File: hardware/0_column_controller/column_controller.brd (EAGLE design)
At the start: 35.6 x 54.6 mm, 45 parts, among them J4 JTAG, U1 ESP-WROVER-32ESP-WROVER-32, U2 3.3V, U3 CP2102N

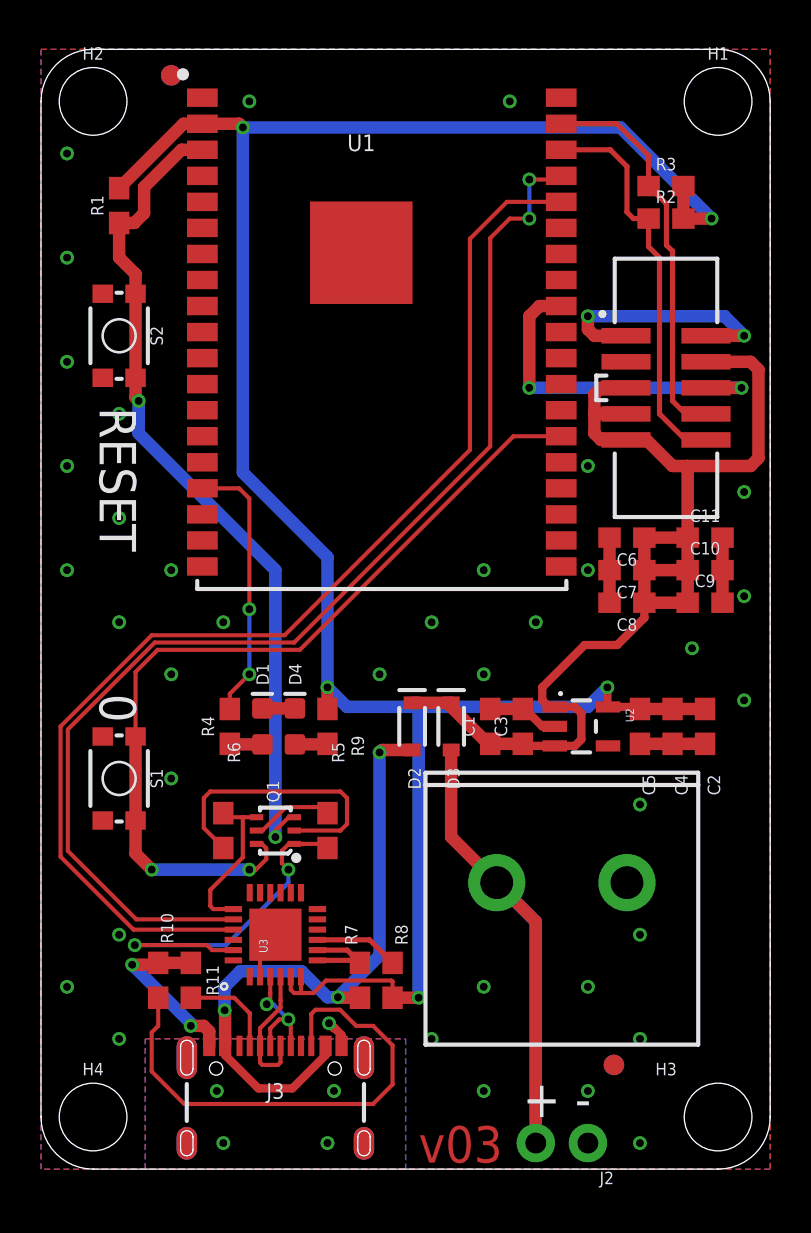
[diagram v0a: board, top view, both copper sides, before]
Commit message: increase standoff size column controller
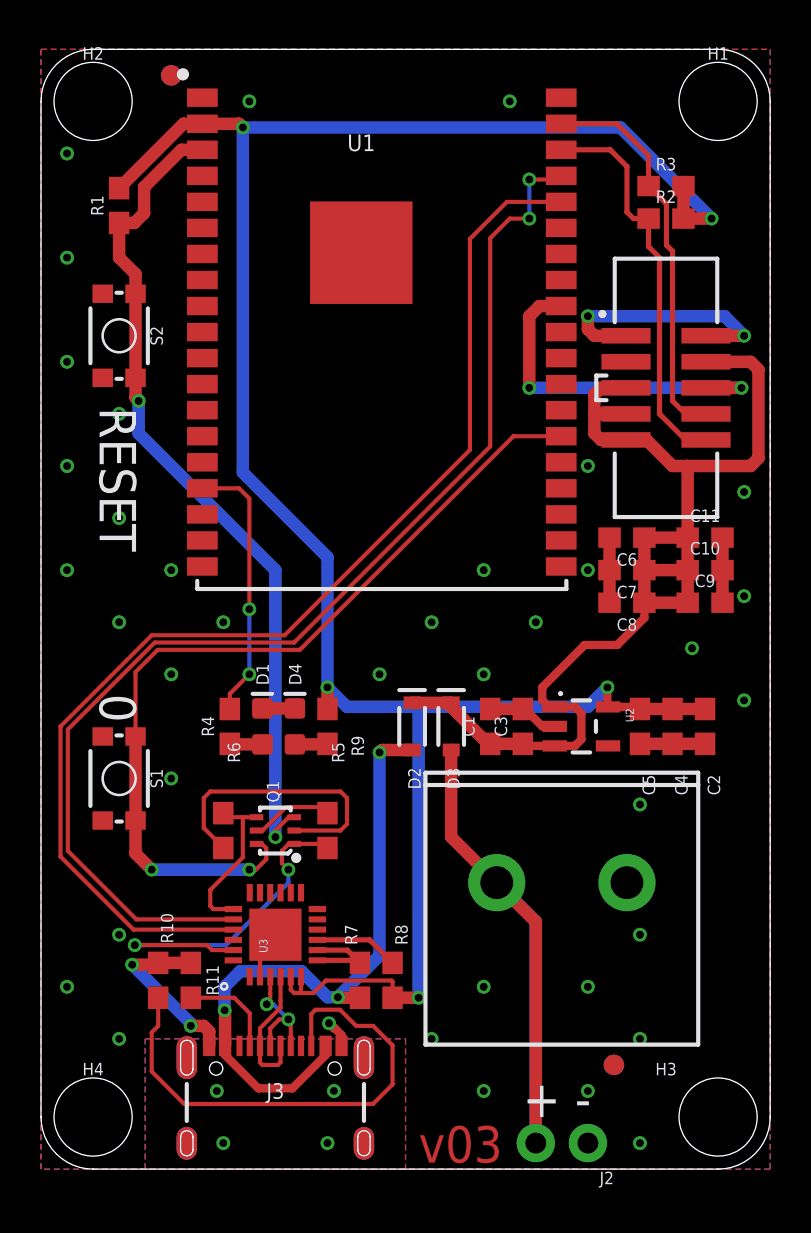
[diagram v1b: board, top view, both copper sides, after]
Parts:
- H1, H2, H3, H4: value STAND-OFF -> STAND-OFF#8; device SparkFun-Hardware:STAND-OFF -> standoff:STAND-OFF-#8
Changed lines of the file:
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@@
 <attribute name="VALUE" x="27.94" y="3.302" size="0.6096" layer="27" font="vector" ratio="20" rot="R180"/>
 </element>
-<element name="H1" library="SparkFun-Hardware" package="STAND-OFF" value="STAND-OFF" x="33.02" y="52.07" smashed="yes">
+<element name="H1" library="standoff" package="STAND-OFF-#8" value="STAND-OFF#8" x="33.02" y="52.07" smashed="yes">
 <attribute name="NAME" x="33.02" y="54.102" size="0.6096" layer="25" font="vector" ratio="20" align="bottom-center"/>
 <attribute name="VALUE" x="29.21" y="46.228" size="0.6096" layer="27" font="vector" ratio="20" align="top-center"/>
 </element>
-<element name="H2" library="SparkFun-Hardware" package="STAND-OFF" value="STAND-OFF" x="2.54" y="52.07" smashed="yes">
+<element name="H2" library="standoff" package="STAND-OFF-#8" value="STAND-OFF#8" x="2.54" y="52.07" smashed="yes">
 <attribute name="NAME" x="2.54" y="54.102" size="0.6096" layer="25" font="vector" ratio="20" align="bottom-center"/>
 <attribute name="VALUE" x="2.54" y="50.038" size="0.6096" layer="27" font="vector" ratio="20" align="top-center"/>
 </element>
-<element name="H3" library="SparkFun-Hardware" package="STAND-OFF" value="STAND-OFF" x="33.02" y="2.54" smashed="yes">
+<element name="H3" library="standoff" package="STAND-OFF-#8" value="STAND-OFF#8" x="33.02" y="2.54" smashed="yes">
 <attribute name="NAME" x="30.48" y="4.572" size="0.6096" layer="25" font="vector" ratio="20" align="bottom-center"/>
 <attribute name="VALUE" x="33.02" y="0.508" size="0.6096" layer="27" font="vector" ratio="20" align="top-center"/>
 </element>
-<element name="H4" library="SparkFun-Hardware" package="STAND-OFF" value="STAND-OFF" x="2.54" y="2.54" smashed="yes">
+<element name="H4" library="standoff" package="STAND-OFF-#8" value="STAND-OFF#8" x="2.54" y="2.54" smashed="yes">
 <attribute name="NAME" x="2.54" y="4.572" size="0.6096" layer="25" font="vector" ratio="20" align="bottom-center"/>
 <attribute name="VALUE" x="2.54" y="0.508" size="0.6096" layer="27" font="vector" ratio="20" align="top-center"/>

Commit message: prepare for v10 generation
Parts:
- J1: device SparkFun-Connectors:1X02_6.35_SCREWTERM -> SparkFun-Connectors:SCREWTERMINAL-3.5MM-4_LOCK
- R2, R3: value 2.2k -> 1k
- R4, R9: value 33 -> 330
- moved J1 4.58 mm to (22.9, 10.2)
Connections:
- net GND: now also J1.3, J1.4; no longer J1.P2
- net VIN: now also J1.1, J1.2; no longer J1.P1
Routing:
- net VIN: track 34.4 -> 38.9 mm
- net GND: vias 42 -> 39
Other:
- board text added: "v10"
- board text removed: "v03"

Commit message: update controller board
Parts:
- removed FRAME1: FRAME-LEDGER, SparkFun-Aesthetics:CREATIVE_COMMONS
- removed J2: (no value), SparkFun-Connectors:1X02_NO_SILK
- added U$1: (no value), buzzard_labels:5V2
- added U$10: (no value), buzzard_labels:SUMMER_202010
- added U$11: (no value), buzzard_labels:#PLAYZEUM#10
- added U$12: (no value), SparkFun-Aesthetics:OSHW-LOGO-M
- added U$2: (no value), buzzard_labels:#GND#6
- added U$3: (no value), buzzard_labels:#13#0
- added U$4: (no value), buzzard_labels:#USER#2
- added U$5: (no value), buzzard_labels:#RESET#3
- added U$6: (no value), ocl_L#PNG:OCL_L#PNG
- added U$7: (no value), buzzard_labels:MUSEUM_OF_BOULDER9
- added U$8: (no value), buzzard_labels:OCLYKE#DEV7
- added U$9: (no value), buzzard_labels:#RAINBOW_FOREST#8
- moved J1 1.80 mm to (21.6, 11.4)
- moved H1 1.27 mm to (33.0, 53.3)
- moved H2 1.27 mm to (2.54, 53.3)
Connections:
- net GND: no longer J2.1
- net VIN: no longer J2.2
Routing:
- net VIN: track 38.9 -> 17.3 mm
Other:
- board size 35.6 x 54.6 mm -> 35.6 x 55.9 mm
- board text removed: "+"
- board text removed: "-"
- board text removed: "0"
- board text removed: "RESET"

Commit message: add frame and organize
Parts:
- added FRAME1: FRAME-LETTER, SparkFun-Aesthetics:CREATIVE_COMMONS

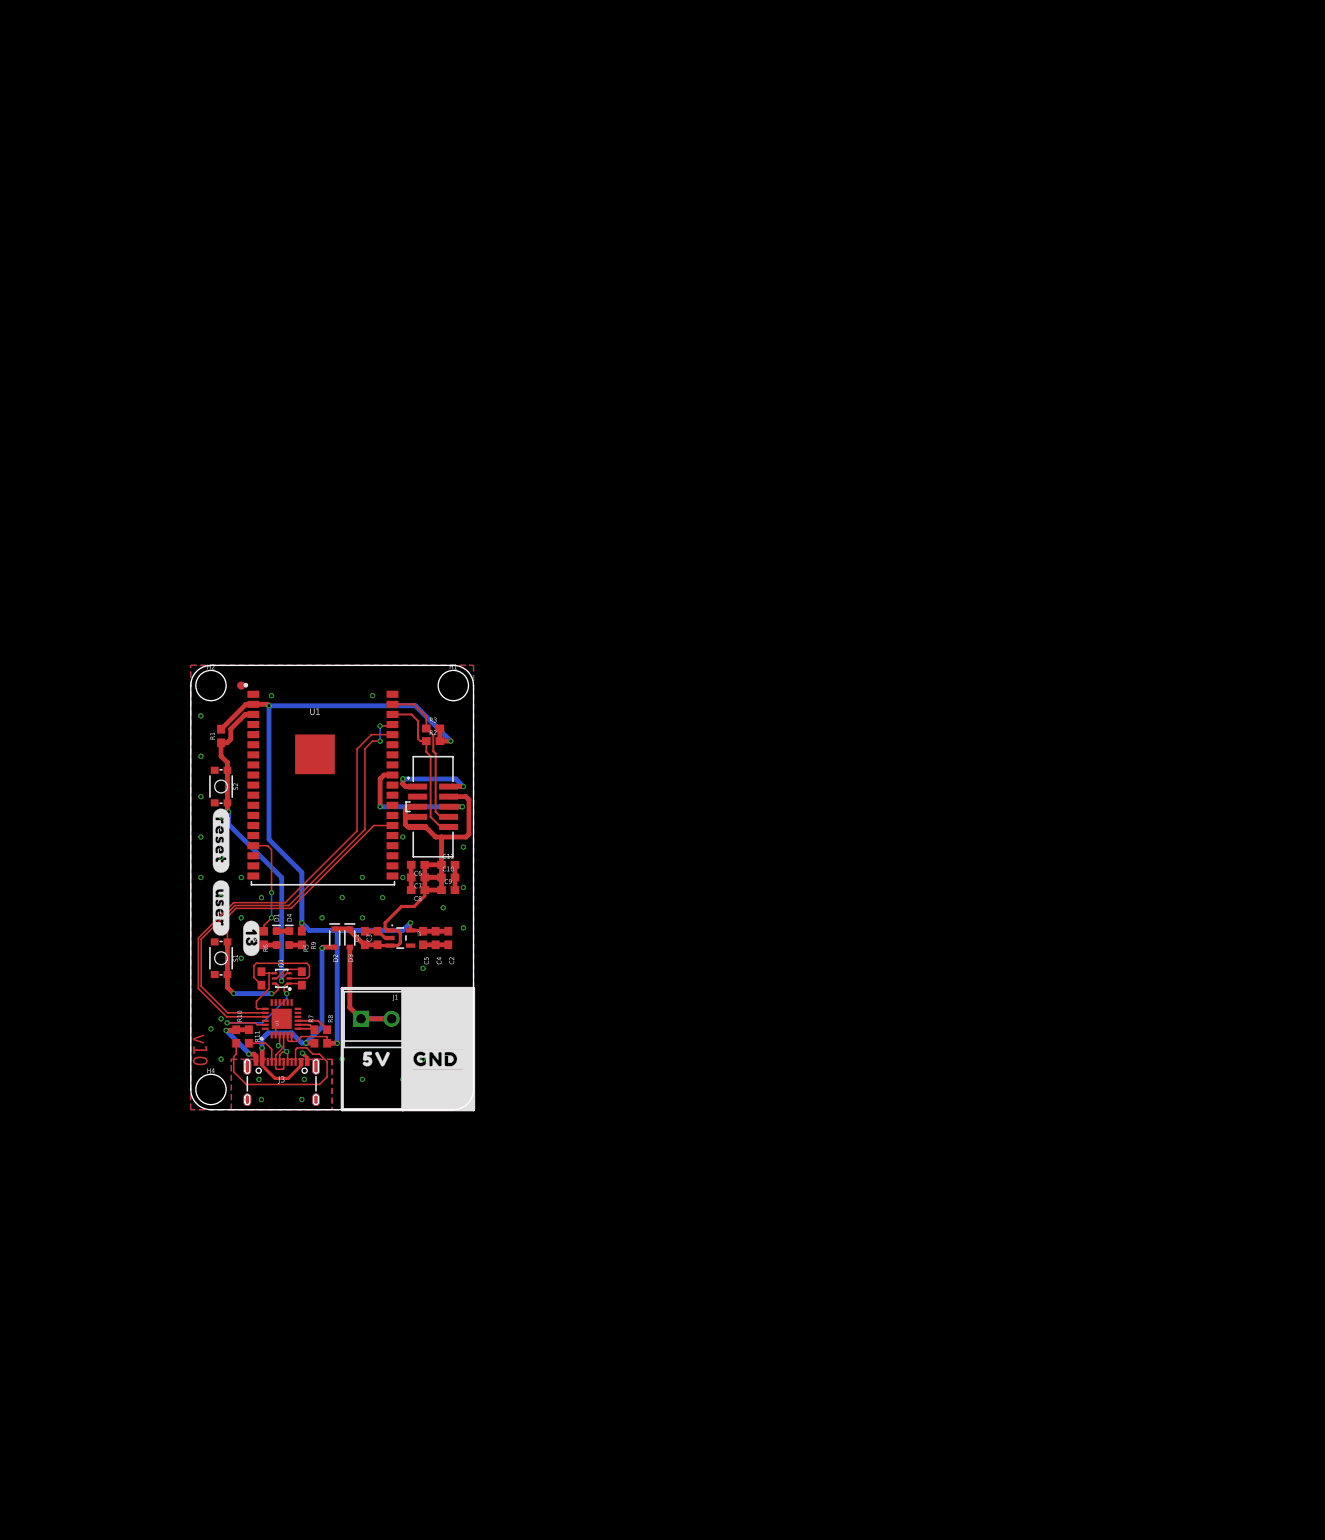
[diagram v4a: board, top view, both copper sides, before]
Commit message: begin change to differential I2C solution
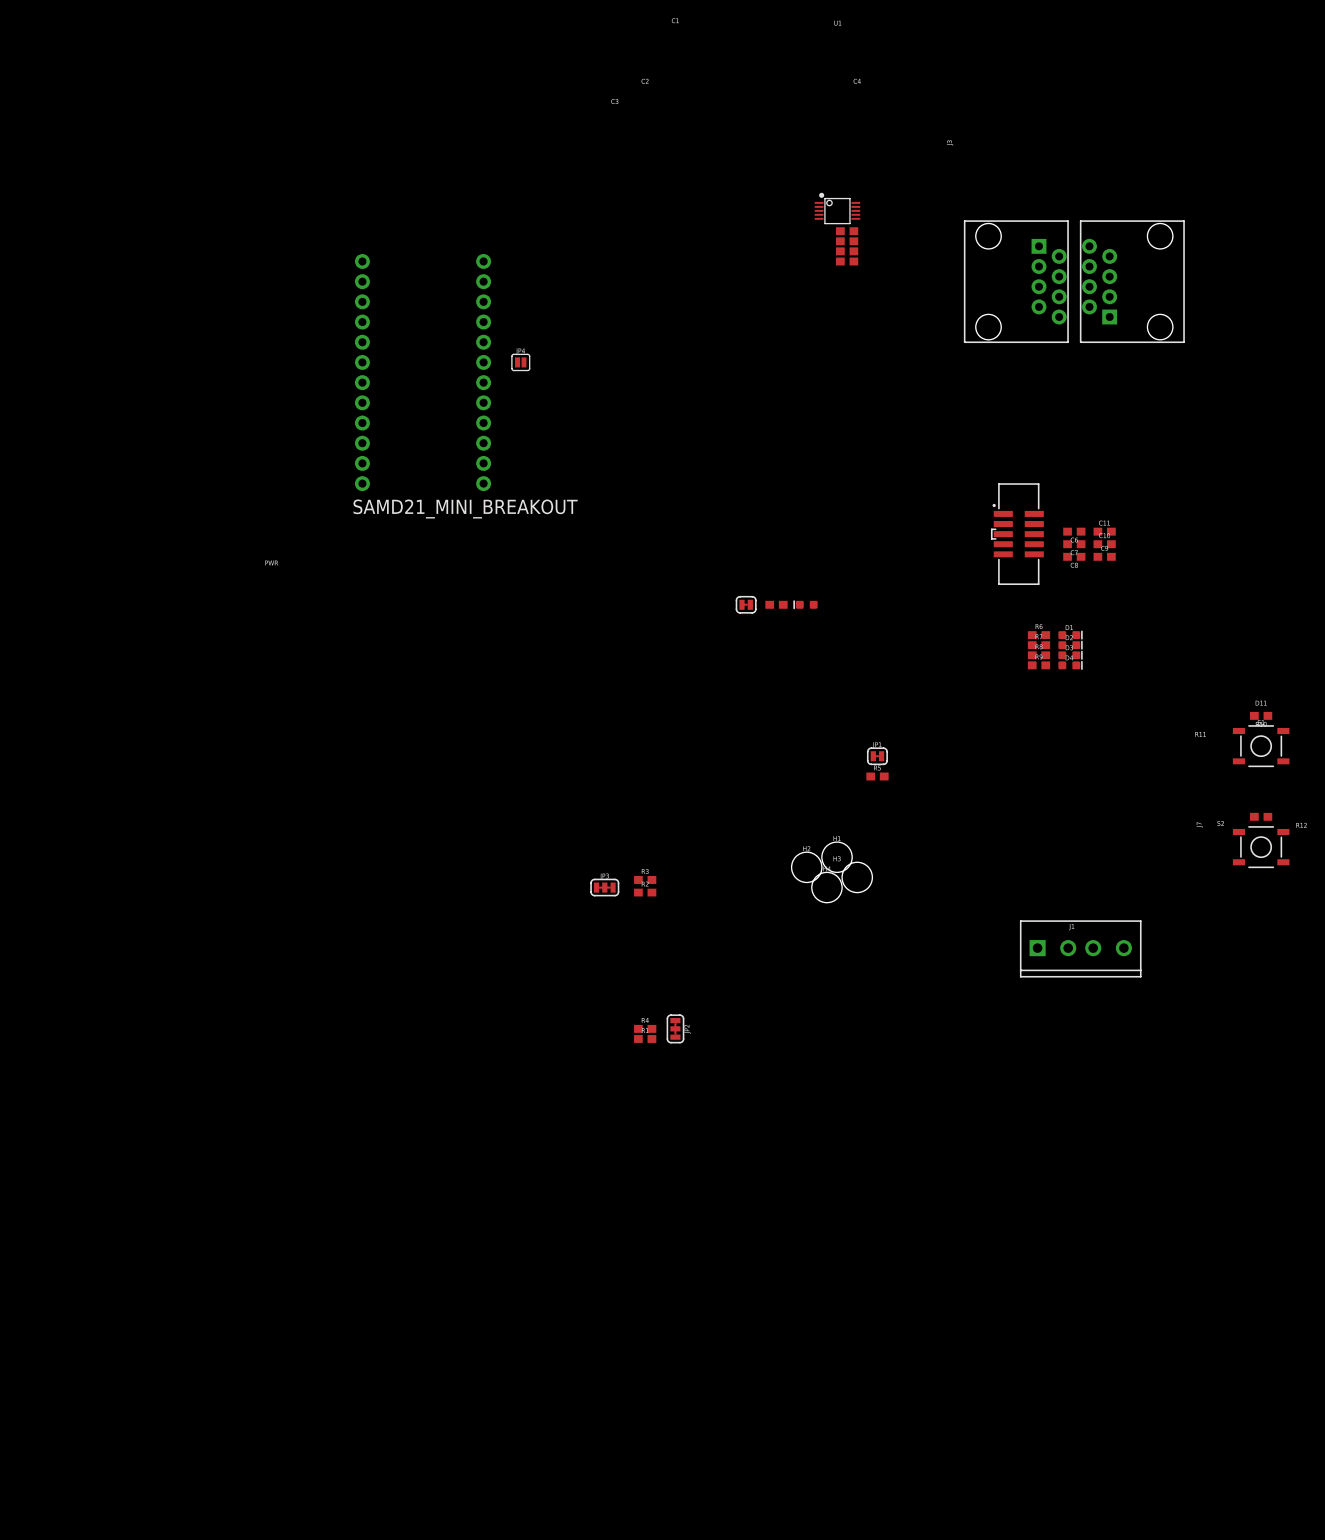
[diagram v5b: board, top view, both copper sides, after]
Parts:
- removed C5: 4.7uF, SparkFun-Capacitors:0603
- removed FD1, FD2, FD3, FD4: FIDUCIAL1X2, SparkFun-Aesthetics:FIDUCIAL-1X2
- removed Q1: (no value), SparkFun-DiscreteSemi:SC70-6
- removed U$1: (no value), buzzard_labels:5V2
- removed U$10: (no value), buzzard_labels:SUMMER_202010
- removed U$11: (no value), buzzard_labels:#PLAYZEUM#10
- removed U$12: (no value), SparkFun-Aesthetics:OSHW-LOGO-M
- removed U$2: (no value), buzzard_labels:#GND#6
- removed U$3: (no value), buzzard_labels:#13#0
- removed U$4: (no value), buzzard_labels:#USER#2
- removed U$5: (no value), buzzard_labels:#RESET#3
- removed U$6: (no value), ocl_L#PNG:OCL_L#PNG
- removed U$7: (no value), buzzard_labels:MUSEUM_OF_BOULDER9
- removed U$8: (no value), buzzard_labels:OCLYKE#DEV7
- removed U$9: (no value), buzzard_labels:#RAINBOW_FOREST#8
- removed U2: 3.3V, SparkFun-IC-Power:SOT23-5
- removed U3: CP2102N, SparkFun-IC-Comms:QFN24
- added D11: RED, SparkFun-LED:LED-0603
- added J7: RJ45, SparkFun-Connectors:RJ45-8
- added JP1, PWR: JUMPER-SMT_2_NC_TRACE_SILK, SparkFun-Jumpers:SMT-JUMPER_2_NC_TRACE_SILK
- added JP2, JP3: JUMPER-SMT_3_2-NC_TRACE_SILK, SparkFun-Jumpers:SMT-JUMPER_3_2-NC_TRACE_SILK
- added JP4: JUMPER-SMT_2_NO_SILK, SparkFun-Jumpers:SMT-JUMPER_2_NO_SILK
- added R12: 1k, SparkFun-Resistors:0603
- added U$13: SAMD21_MINI_BREAKOUT, SparkFun-Boards:SAMD21_MINI_BREAKOUT
- D1: value 13 -> BLUE
- D2, D3: value 3A/10V/280mV -> BLUE; device SparkFun-DiscreteSemi:SOD-323 -> SparkFun-LED:LED-0603
- D4: value POWER -> BLUE
- J3: value (none) -> RJ45; device SparkFun-Connectors:USB-C-16P -> SparkFun-Connectors:RJ45-8
- R1, R6: value 10k -> 1k
- R10, R11: value 5.1k -> 1k
- R4, R9: value 330 -> 1k
- R5: value 10k -> DNP
- R7: value 10 -> 1k
- S1: value Button 0 -> MOMENTARY-SWITCH-SPST-SMD-5.2MM-TALL; device SparkFun-Switches:TACTILE_SWITCH_SMD_4.6X2.8MM -> SparkFun-Switches:TACTILE_SWITCH_SMD_5.2MM
- S2: value !RESET -> MOMENTARY-SWITCH-SPST-SMD-5.2MM-TALL; device SparkFun-Switches:TACTILE_SWITCH_SMD_4.6X2.8MM -> SparkFun-Switches:TACTILE_SWITCH_SMD_5.2MM
- U1: value ESP-WROVER-32ESP-WROVER-32 -> PCA9615; device SparkFun-RF:ESP-WROVER-32 -> SparkFun-IC-Comms:TSSOP10
- moved R10 135.1 mm to (134.6, 49.5), turned to 180 degrees
- moved S1 133.5 mm to (134.6, 45.7), turned to 0 degrees
- moved J3 132.2 mm to (100.3, 104.1), turned to 270 degrees
- moved S2 131.0 mm to (134.6, 33.0), turned to 0 degrees
- moved C1 107.6 mm to (82.5, 110.5), turned to 0 degrees
- moved R6 106.9 mm to (106.7, 59.7), turned to 0 degrees
- moved D1 106.7 mm to (110.5, 59.7), turned to 0 degrees
- moved C3 104.6 mm to (82.5, 108.0), turned to 0 degrees
- moved D4 103.9 mm to (110.5, 55.9), turned to 0 degrees
- moved R7 103.6 mm to (106.7, 58.4), turned to 0 degrees
- moved C4 101.8 mm to (82.5, 109.2), turned to 0 degrees
- moved R8 101.6 mm to (106.7, 57.1), turned to 0 degrees
- moved D2 99.5 mm to (110.5, 58.4), turned to 0 degrees
- moved R9 98.8 mm to (106.7, 55.9), turned to 0 degrees
- moved C2 98.8 mm to (82.5, 106.7), turned to 0 degrees
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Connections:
- removed net !RESET: Q1.3, R1.1, S2.3, S2.4, U1.P$3
- removed net 0: Q1.6, S1.3, S1.4, U1.P$25
- removed net 13: R4.2, U1.P$16
- removed net DTR: Q1.1, R5.2, U3.23
- removed net N$11: J3.B5, R10.2
- removed net RTS: Q1.4, R6.2, U3.19
- removed net RX: U1.P$35, U3.20
- removed net SCL: J4.10, R2.1, U1.P$36
- removed net SDA: J4.8, R3.1, U1.P$37
- removed net SHLD: J3.SHLD1, J3.SHLD2, J3.SHLD3, J3.SHLD4, J3.SHLD5, J3.SHLD6, J3.SHLD7, J3.SHLD8
- removed net TX: U1.P$34, U3.21
- removed net VIN: D3.A, J1.1, J1.2
- removed net V_USB: D2.A, J3.VBUS1, J3.VBUS2, R7.1
- new net B0: R10.2, S1.1, U$13.PA18
- new net B1: R12.2, S2.1, U$13.PA19
- new net DSCL_N: J3.1, J7.1, U1.6
- new net DSCL_P: J3.2, J7.2, U1.7
- new net DSDA_N: J3.7, J7.7, U1.9
- new net DSDA_P: J3.8, J7.8, U1.8
- new net LED0: R6.1, U$13.PA10
- new net LED1: R7.1, U$13.PA11
- new net LED2: R8.1, U$13.PA14
- new net LED3: R9.1, U$13.PA15
- new net N$13: D11.C, R11.1
- new net N$14: PWR.2, R11.2
- new net N$9: D2.A, R7.2
- new net PCA_EN: JP4.2, U1.3
- new net SCL_COLUMN: J4.10, R2.1, U$13.PA09
- new net SCL_NETWORK: R1.1, U$13.PA17, U1.4
- new net SDA_COLUMN: J4.8, R3.1, U$13.PA08
- new net SDA_NETWORK: R4.1, U$13.PA16, U1.2
- net 3.3V: now also C1.1, C3.1, D11.A, JP2.2, JP3.2, R10.1, R12.1, U$13.3V3, U1.1, U1.10; no longer C5.1, R1.2, R2.2, R3.2, R8.2, R9.2, U1.P$2, U2.5, U3.5, U3.6
- net 5V: now also J1.3, J1.4, J3.3, J7.3, U$13.AREF, U$13.VIN; no longer C1.1, C3.1, D2.C, D3.C, U2.1, U2.3
- net DOUT: now also JP1.2, R5.2; no longer U1.P$30
- net GND: now also D2.C, D3.C, J1.1, J1.2, J3.6, J7.6, PWR.1, S1.3, S2.3, U$13.GND, U$13.GND1, U1.5; no longer C5.2, J1.3, J1.4, J3.GND, J3.GND2, R10.1, R11.1, S1.1, S1.2, S2.1, S2.2, U1.P$1, U1.P$15, U1.P$38, U1.P$39, U2.2, U3.2, U3.PAD
- net N$1: now also JP1.1, R5.1, U$13.PA20; no longer J3.A7, J3.B7, U3.4
- net N$10: now also JP4.1, U$13.PB09; no longer J3.A5, R11.2
- net N$2: now also JP2.3, R1.2; no longer J3.A6, J3.B6, U3.3
- net N$3: now also JP2.1, R4.2; no longer Q1.2, R6.1
- net N$4: now also JP3.3, R2.2; no longer D1.A, R4.1
- net N$5: now also JP3.1, R3.2; no longer Q1.5, R5.1
- net N$6: now also D1.A, R6.2; no longer R7.2, U3.7, U3.8
- net N$7: now also D4.A, R9.2; no longer R8.1, U3.9
- net N$8: now also D3.A, R8.2; no longer D4.A, R9.1
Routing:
- net 3.3V: track 108.3 -> 0.00 mm, vias 5 -> 0
- net 5V: track 57.7 -> 0.00 mm
- net RX: track 57.7 -> 0.00 mm, vias 2 -> 0
- net TX: track 57.3 -> 0.00 mm
- net 0: track 42.4 -> 0.00 mm, vias 2 -> 0
- net !RESET: track 41.2 -> 0.00 mm, vias 2 -> 0
- net GND: track 40.2 -> 0.00 mm, vias 39 -> 0
- net V_USB: track 31.9 -> 0.00 mm, vias 3 -> 0
- net N$11: track 24.8 -> 0.00 mm
- net SCL: track 19.5 -> 0.00 mm
- net SDA: track 19.2 -> 0.00 mm
- net DTR: track 17.8 -> 0.00 mm, vias 2 -> 0
- net DOUT: track 17.3 -> 0.00 mm, vias 2 -> 0
- net VIN: track 17.3 -> 0.00 mm
- net N$3: track 14.1 -> 0.00 mm
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- removed copper zone on layer 1, net GND
- removed copper zone on layer 16, net GND
- removed copper zone on layer 1, net SHLD
- removed copper zone on layer 16, net SHLD
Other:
- board outline removed
- board text added: "oclyke"
- board text removed: "v10"
